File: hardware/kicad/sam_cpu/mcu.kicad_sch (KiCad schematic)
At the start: 44 parts, among them J19 USB-C (to Pi), J20 SWD, J21 Raspberry Pi 40-pin, SW1 RESET, SW2 BOOTSEL, U4 RP2354B, U5 TPS3808G33, Y1 12MHz

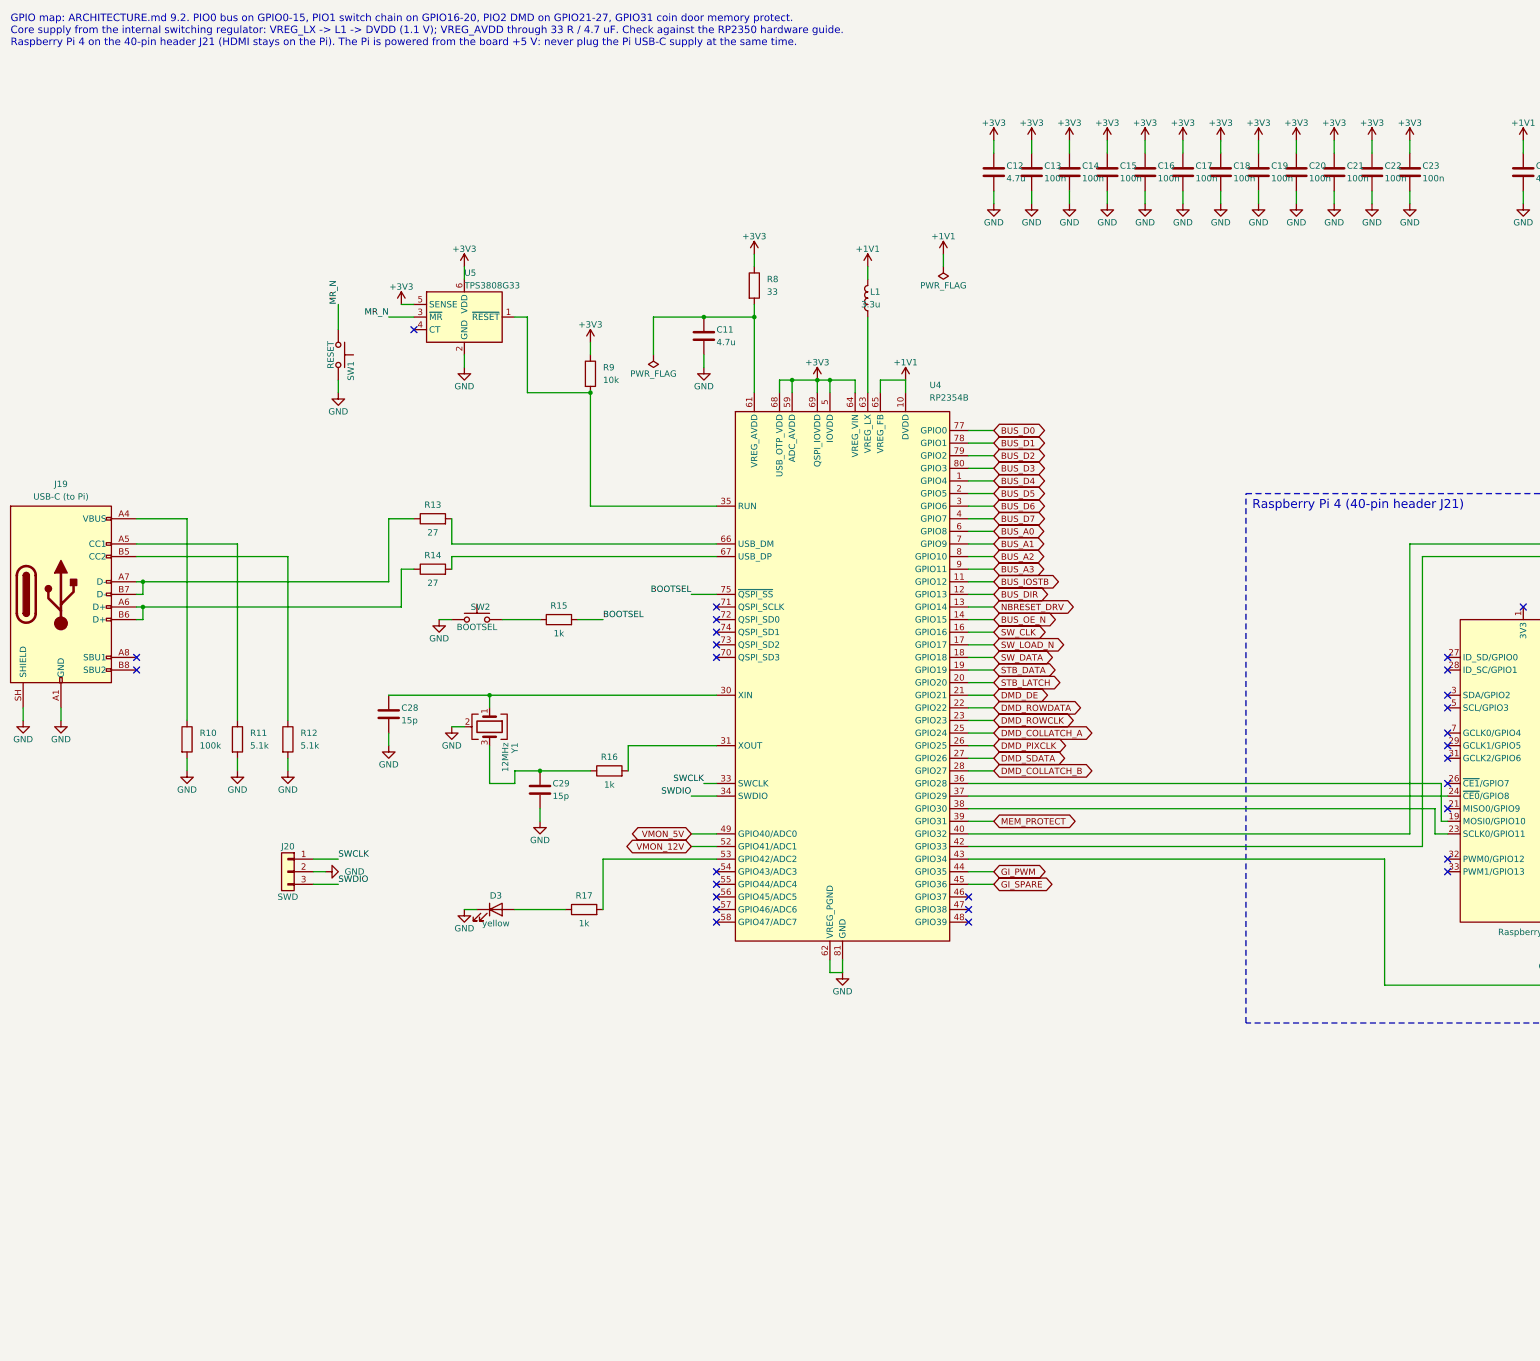
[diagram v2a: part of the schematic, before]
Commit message: Add RTC, test points and stereo speaker connector; place all parts on 2 layers
Schematic: DS3231MZ real-time clock on the Pi I2C1 with a CR2032 holder,
22 test points (rails, bus, strobes, switch chain, VREF, DAC outputs) and
J22, a second KK-396 speaker connector with L and R as separate pairs.
ERC 0 errors, generated netlist matches the intended nets.

PCB: 2 copper layers. The RP2354B sits near J9 with its USB-C on the top
edge 13 mm from the USB pins; decoupling, regulator and crystal parts on
their pins; every other part grouped by sheet next to its connector, low
parts only under the Pi. J17 and J22 on the right edge; Pi and J5 12 mm
lower to fit the audio parts.

Co-Authored-By: Claude Opus 5.5 (1M context) <noreply@anthropic.com>
Claude-Session: https://claude.ai/code/session_01ExuDVoDDDHhVWjb8EwVzYb
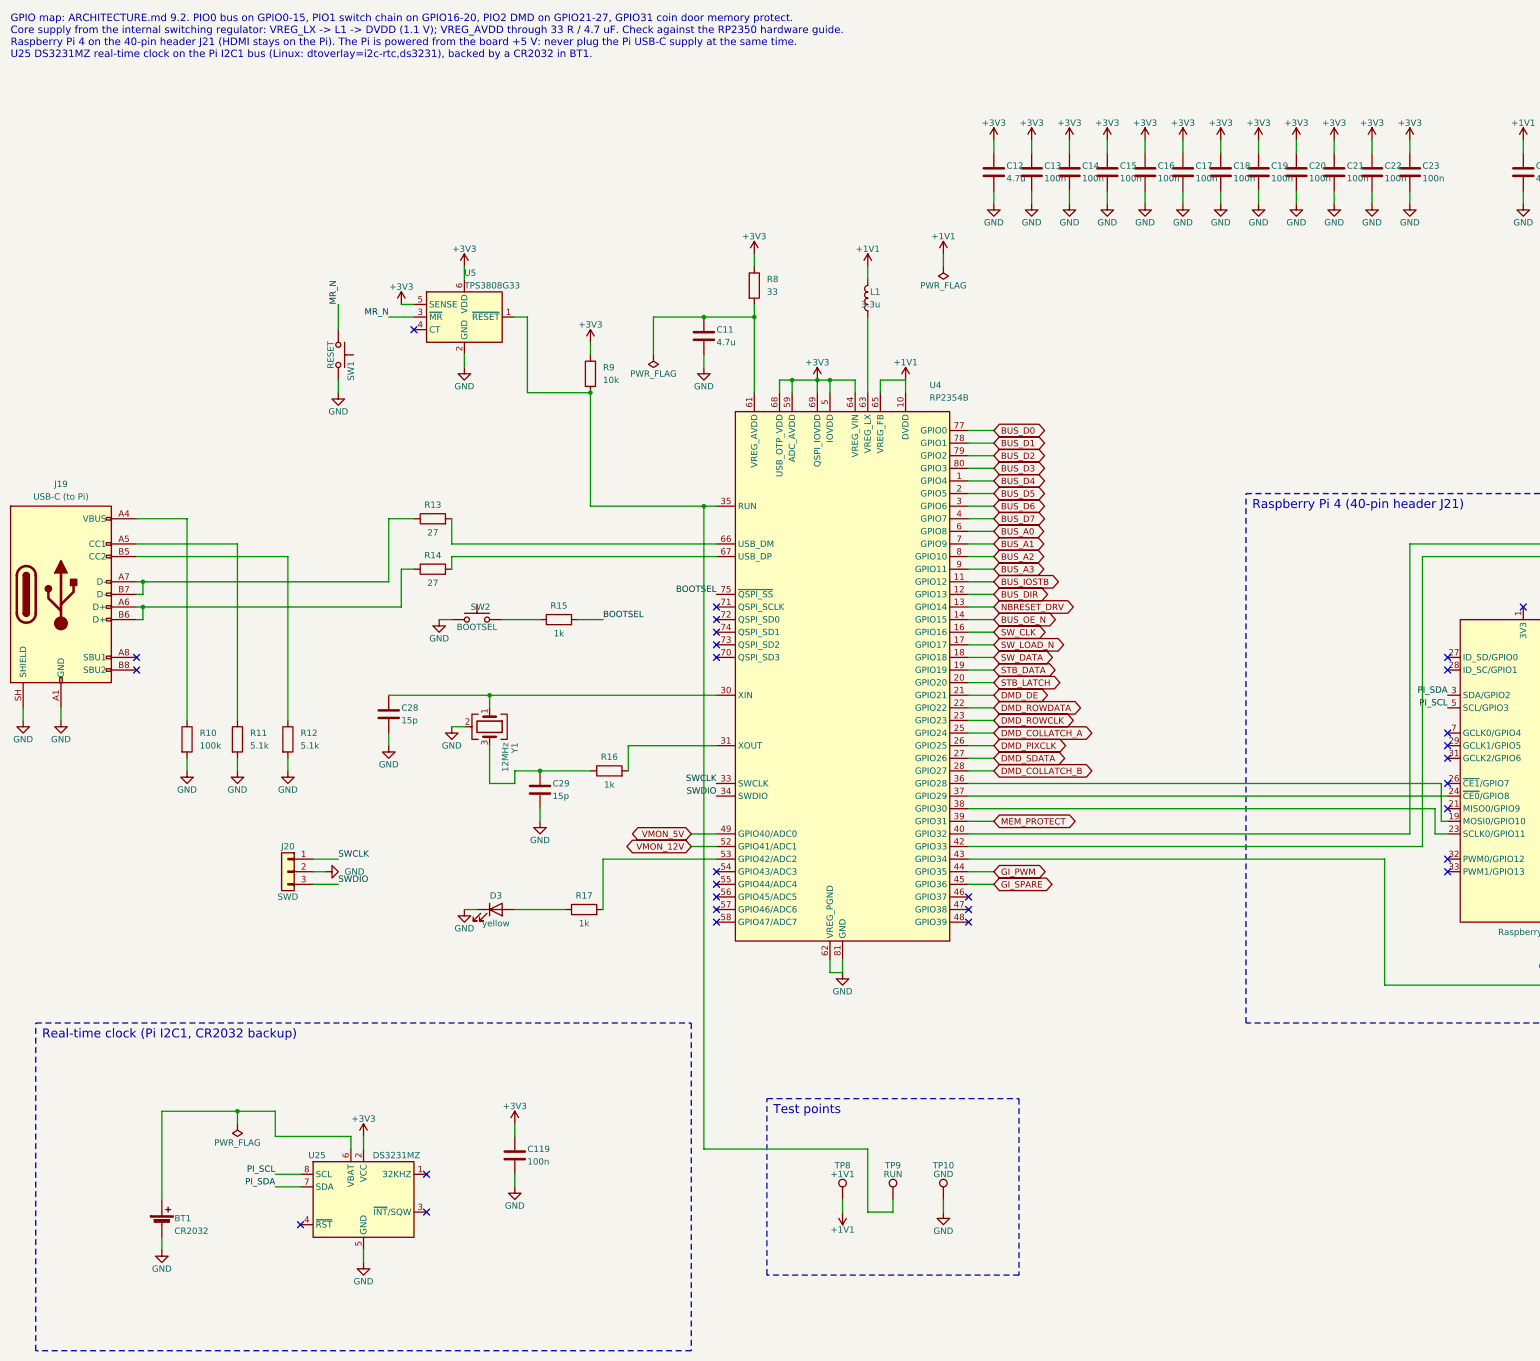
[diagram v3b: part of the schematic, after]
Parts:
- added BT1: CR2032, Battery:BatteryHolder_Keystone_3034_1x20mm, symbol Device:Battery_Cell
- added C119: 100n, Capacitor_SMD:C_0603_1608Metric, symbol Device:C
- added TP10: GND, TestPoint:TestPoint_Pad_D1.5mm, symbol Connector:TestPoint
- added TP8: +1V1, TestPoint:TestPoint_Pad_D1.5mm, symbol Connector:TestPoint
- added TP9: RUN, TestPoint:TestPoint_Pad_D1.5mm, symbol Connector:TestPoint
- added U25: DS3231MZ, Package_SO:SOIC-8_3.9x4.9mm_P1.27mm, symbol Timer_RTC:DS3231MZ
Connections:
- net +1V1: now also TP8.1
- net +3V3: now also C119.1, U25.2 (VCC)
- net GND: now also BT1.2 (-), C119.2, TP10.1, U25.5 (GND)
- net at R9.2, U4.35 (RUN), U5.1 (~{RESET}): now also TP9.1
- net PI_SDA: now reaches J21.3 (SDA/GPIO2)
- net PI_SDA: now also U25.7 (SDA)
- net PI_SCL: now reaches J21.5 (SCL/GPIO3)
- net PI_SCL: now also U25.8 (SCL)
- new net: BT1.1 (+), U25.6 (VBAT)
- no-connect marks 32 -> 33
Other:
- note added: "Real-time clock (Pi I2C1, CR2032 backup)"
- note added: "Test points"

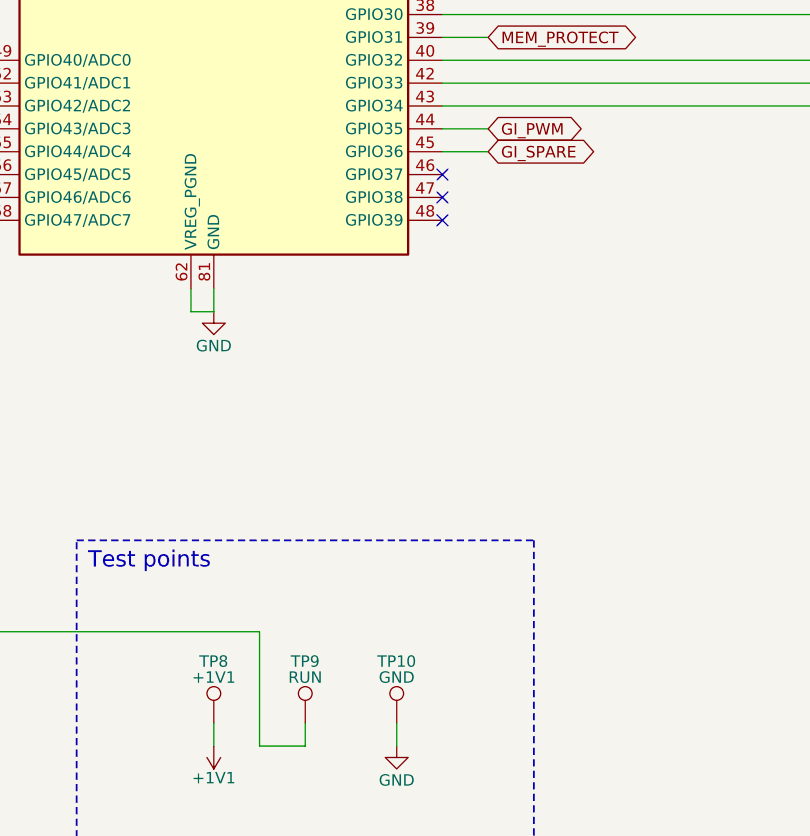
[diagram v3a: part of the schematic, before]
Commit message: Audio on external 12 V with TDA7297 stereo + subwoofer amps, NCP1117, guide regulator layout
- Remove the +-12 V input from J11; J23 external +12 V with polyfuse and TVS
- Replace the two TDA2030A with a TDA7297 bridge amp for left/right (J10, J22)
  and a second TDA7297 for the subwoofer (J24), fed by an (L+R)/2 110 Hz
  Sallen-Key low-pass (OPA1678); shared standby and RP2354B-controlled mute
- AMS1117 -> NCP1117-3.3 (ceramic-stable, as in the RP2350 guide), 10 uF 1206
- L1 and crystal part numbers from the RP2350 hardware guide
- Place the core regulator parts by hand following the Pico 2 layout; amps in a
  row with a heatsink keep-out; J23/J22/J24 on the right edge

Co-Authored-By: Claude Opus 5.5 (1M context) <noreply@anthropic.com>
Claude-Session: https://claude.ai/code/session_01ExuDVoDDDHhVWjb8EwVzYb
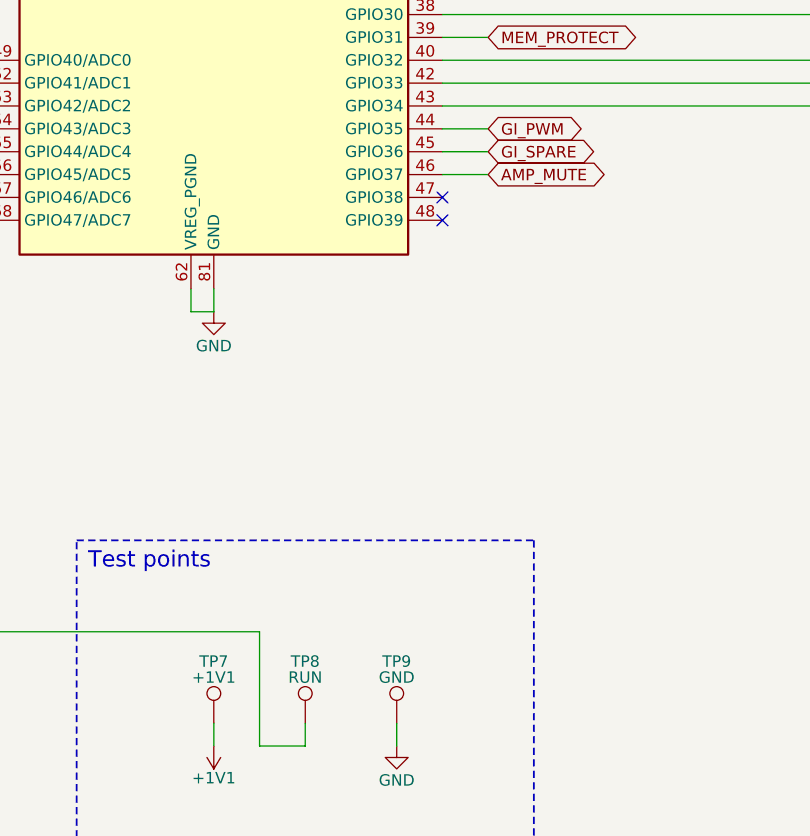
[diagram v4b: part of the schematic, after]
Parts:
- removed TP10: GND, TestPoint:TestPoint_Pad_D1.5mm, symbol Connector:TestPoint
- added TP7: +1V1, TestPoint:TestPoint_Pad_D1.5mm, symbol Connector:TestPoint
- L1: MPN (none) -> Abracon AOTA-B201610S3R3-101-T (polarity dot as on Pico 2)
- TP8: value +1V1 -> RUN
- TP9: value RUN -> GND
- Y1: MPN (none) -> Abracon ABM8-272-T3
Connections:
- net +1V1: now also TP7.1; no longer TP8.1
- net GND: now also TP9.1
- net at R9.2, U4.35 (RUN), U5.1 (~{RESET}): now also TP8.1; no longer TP9.1
- net AMP_MUTE: now reaches U4.46 (GPIO37)
- no-connect marks 33 -> 32
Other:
- moved on the sheet: TP8, TP9

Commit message: Add two HD DMD panels on a PIO parallel bus (incremental edit)
RP2354B GPIO20-36 drive two HUB75 panels (J25/J26) through 3 x 74AHCT245
with shared CLK/LAT/OE and A/B row lines; J5 shares DMD_D0-D6. The 165
load and 595 latch share GPIO17; coin door moves to a 7th 165 (U30),
LED_STATUS and GI_SPARE to a new first 595 (U31). Board widened to 142 mm
below the Pi. Sheets and board edited in place via tools/changes, no
existing footprint moved.

Co-Authored-By: Claude Opus 5.5 (1M context) <noreply@anthropic.com>
Claude-Session: https://claude.ai/code/session_01ExuDVoDDDHhVWjb8EwVzYb
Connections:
- net AMP_MUTE: now also U4.48 (GPIO39); no longer U4.46 (GPIO37)
- net GI_PWM: now also U4.47 (GPIO38); no longer U4.44 (GPIO35)
- net VMON_12V: now also U4.58 (GPIO47/ADC7); no longer U4.52 (GPIO41/ADC1)
- net VMON_5V: now also U4.57 (GPIO46/ADC6); no longer U4.49 (GPIO40/ADC0)
- net FRAME_SCK: now reaches U4.53 (GPIO42/ADC2)
- net FRAME_SCK: now also J21.23 (SCLK0/GPIO11); no longer R17.2
- net RP_IRQ_N: now reaches J21.16 (GPIO23), R22.2
- net RP_IRQ_N: now also U4.46 (GPIO37); no longer U4.43 (GPIO34)
- net DMD_D8: now reaches U4.36 (GPIO28)
- net DMD_D8: no longer J21.19 (MOSI0/GPIO10)
- net DMD_D10: now reaches U4.38 (GPIO30)
- net DMD_D10: no longer J21.23 (SCLK0/GPIO11)
- net DMD_D9: now reaches U4.37 (GPIO29)
- net DMD_D9: no longer J21.24 (~{CE0}/GPIO8)
- net DMD_CLK: now reaches U4.40 (GPIO32)
- net DMD_CLK: no longer R19.2
- net DMD_LAT: now reaches U4.42 (GPIO33)
- net DMD_LAT: no longer R18.2
- net RP_UART_TX: now reaches U4.55 (GPIO44/ADC4)
- net RP_UART_TX: now also R19.2
- net RP_UART_RX: now reaches U4.56 (GPIO45/ADC5)
- net RP_UART_RX: now also R18.2
- net DMD_COLLATCH_A renamed DMD_D4
- net DMD_COLLATCH_B renamed DMD_D7
- net DMD_DE renamed DMD_D1
- net DMD_PIXCLK renamed DMD_D5
- net DMD_ROWCLK renamed DMD_D3
- net DMD_ROWDATA renamed DMD_D2
- net DMD_SDATA renamed DMD_D6
- net GI_SPARE renamed DMD_B
- net MEM_PROTECT renamed DMD_D11
- net STB_LATCH renamed DMD_D0
- new net DMD_A: U4.44 (GPIO35)
- new net DMD_OE: U4.43 (GPIO34)
- new net FRAME_CS_N: J21.24 (~{CE0}/GPIO8), U4.52 (GPIO41/ADC1)
- new net FRAME_MOSI: J21.19 (MOSI0/GPIO10), U4.49 (GPIO40/ADC0)
- new net LED_STATUS: R17.2
- no-connect marks 32 -> 26
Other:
- note added: "GPIO map: ARCHITECTURE.md 9.2. PIO0 bus on GPIO0-15, PIO1 switch chain on GPIO16-20, PIO2 drives two HD DMD panels on GPIO20-36 (data 20-31, CLK, LAT, OE, A, B); the original DMD (J5) shares GPIO20-26. Frames from the Pi on SPI1 (GPIO40-42), UART0 on GPIO44-45, ADC monitors on GPIO46-47, GPIO43 spare. Coin door, status LED and GI_SPARE moved onto the switch chain. Core supply from the internal sw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"
- note removed: "GPIO map: ARCHITECTURE.md 9.2. PIO0 bus on GPIO0-15, PIO1 switch chain on GPIO16-20, PIO2 DMD on GPIO21-27, GPIO31 coin door memory protect. Core supply from the internal switching regulator: VREG_LX -> L1 -> DVDD (1.1 V); VREG_AVDD through 33 R / 4.7 uF. Check against the RP2350 hardware guide. Raspberry Pi 4 on the 40-pin header J21 (HDMI stays on the Pi). The Pi is powered from the board +5 V: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"
